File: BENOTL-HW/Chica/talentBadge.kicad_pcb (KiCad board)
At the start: 2 copper layers, 96.6 x 102.2 mm, 65 parts, among them P1 USB_A, P2 OLED, P3 Batt, P4 PS, Q1 MMBT3904, Q2 MMBT3904, Q3 IR phototransistor, SW1 B1, SW2 B2, SW3 RST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

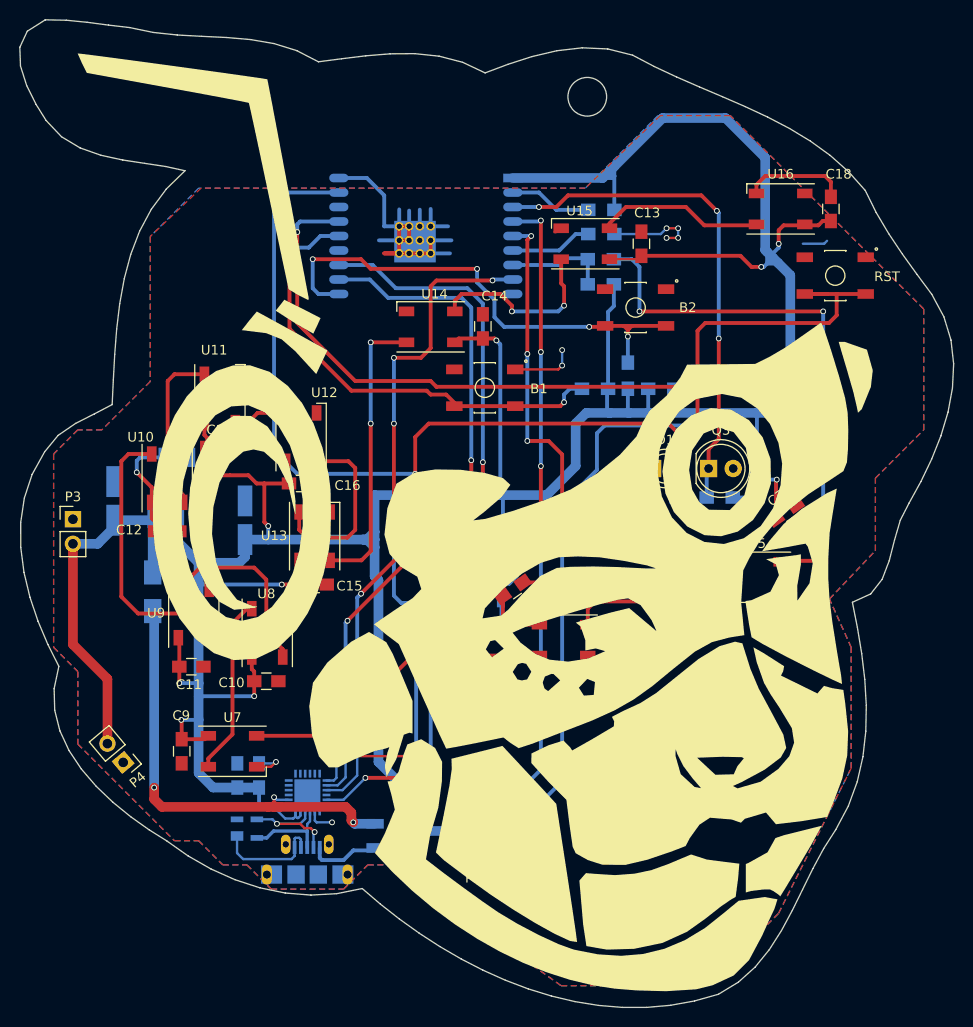
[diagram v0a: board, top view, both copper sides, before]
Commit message: Chica - battery
Se agrega holders para baterias AAA.
Se mueven transistores de programacion y las resistencias de los leds ir.

Pantalla principal muestra 1 unconnected, DRC muestra no unconected.
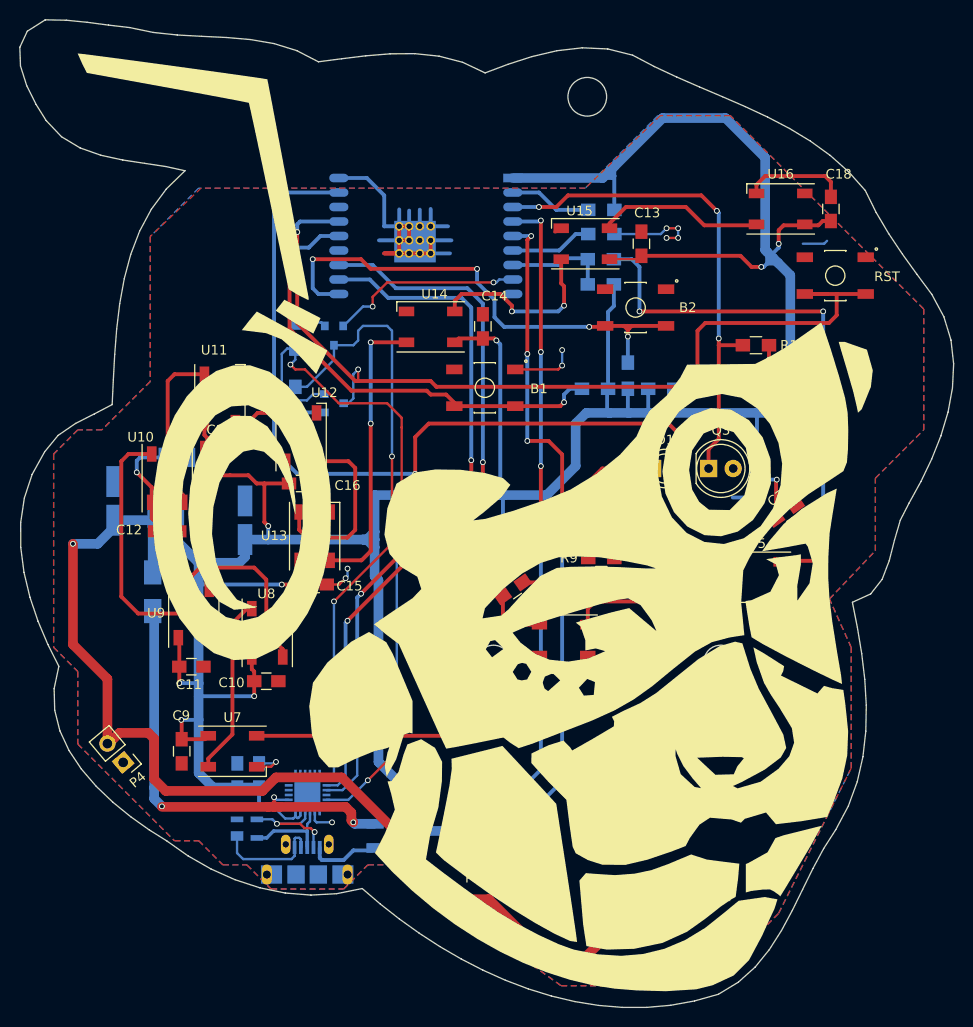
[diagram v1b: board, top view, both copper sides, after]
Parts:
- P3: footprint Pin_Headers:Pin_Header_Straight_1x02_Pitch2.54mm -> talentBadge:Keystone_2479_3xAAA; moved to B.Cu
- R14, R9: moved to F.Cu
- moved P3 77.3 mm to (182.0, 129.0), turned to 90 degrees
- moved G*** 63.8 mm to (130.8, 68.0)
- moved G*** 57.2 mm to (197.8, 80.0)
- moved G*** 54.3 mm to (189.6, 64.6)
- moved G*** 53.6 mm to (177.8, 53.4)
- moved R5 33.2 mm to (138.0, 71.5), turned to 270 degrees
- moved R4 31.1 mm to (138.0, 78.2), turned to 90 degrees
- moved Q2 28.4 mm to (142.0, 71.5), turned to 270 degrees
- moved Q1 25.5 mm to (142.0, 78.5), turned to 0 degrees
- moved svg2mod 20.5 mm to (138.8, 100.4)
- moved R14 16.2 mm to (185.7, 72.5)
- moved REF*** 14.1 mm to (157.2, 72.8)
- moved R9 8.98 mm to (169.7, 94.5)
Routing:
- net Net-(C3-Pad1): track 36.6 -> 108.2 mm, vias 0 -> 1
- net RST: track 134.5 -> 102.7 mm
- net RTS: track 38.1 -> 67.8 mm, vias 4 -> 2
- net GPIO0: track 47.0 -> 20.1 mm, vias 4 -> 2
- net DTR: track 42.6 -> 67.3 mm, vias 2 -> 4
- net Net-(D1-Pad1): track 3.09 -> 15.4 mm
- net Net-(U6-Pad2): track 32.7 -> 36.6 mm
- net GND: track 100.0 -> 103.3 mm, vias 10 -> 12
- net +3V3: track 412.0 -> 413.2 mm, vias 11 -> 12

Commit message: Chica - I2C pullupt
Se agregan pullups a linea i2c para display.
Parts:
- added R10: 10k, Resistors_SMD:R_0805_HandSoldering, B.Cu at (168.9, 74.8)
- added R11: 10k, Resistors_SMD:R_0805_HandSoldering, B.Cu at (169.7, 68.6)
- moved C14 0.15 mm to (157.4, 70.4)
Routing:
- net GND: track 103.3 -> 115.5 mm, vias 12 -> 16
- net SCL: track 71.5 -> 77.9 mm
- net SDA: track 67.3 -> 73.4 mm, vias 4 -> 5
- net +3V3: track 413.2 -> 415.4 mm
- net (no net): vias 0 -> 2
